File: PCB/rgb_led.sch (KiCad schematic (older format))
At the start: 4 parts

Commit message: PCB Edge.Cuts Defined
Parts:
- removed R? (x3): Resistor, symbol Resistor
- added C4: Capacitor, local:SMD-0805, symbol Capacitor
- D0: renamed from D?; footprint (none) -> local:T-1_5mm
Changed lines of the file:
@@
 EELAYER 26 0
 EELAYER END
-$Descr A4 11693 8268
+$Descr A 11000 8500
 encoding utf-8
-Sheet 5 5
-Title ""
-Date ""
-Rev ""
-Comp ""
+Sheet 12 20
+Title "Christmas Tree Disco"
+Date "2017-08-01"
+Rev "01"
+Comp "www.GitHub.com/Cryochasm"
 Comment1 ""
 Comment2 ""
@@
 $EndDescr
 $Comp
-L Resistor R?
-U 1 1 5980A851
-P 5200 3600
-F 0 "R?" H 5200 3450 50  0000 L CNN
-F 1 "Resistor" H 5050 3525 50  0000 L CNN
-F 2 "" H 5200 3600 60  0001 C CNN
-F 3 "" H 5200 3600 60  0001 C CNN
-F 4 "?" H 5200 3600 60  0001 C CNN "MPN"
-F 5 "?" H 5200 3600 60  0001 C CNN "Description"
-F 6 "Yes" H 5200 3600 60  0001 C CNN "Included in BOM"
-	1    5200 3600
-	0    1    1    0
-$EndComp
-$Comp
-L Resistor R?
-U 1 1 5980B065
-P 5400 3600
-F 0 "R?" H 5400 3500 50  0000 L CNN
-F 1 "Resistor" H 5275 3525 50  0000 L CNN
-F 2 "" H 5400 3600 60  0001 C CNN
-F 3 "" H 5400 3600 60  0001 C CNN
-F 4 "?" H 5400 3600 60  0001 C CNN "MPN"
-F 5 "?" H 5400 3600 60  0001 C CNN "Description"
-F 6 "Yes" H 5400 3600 60  0001 C CNN "Included in BOM"
-	1    5400 3600
-	0    1    1    0
-$EndComp
-$Comp
-L Resistor R?
-U 1 1 5980B07B
-P 5600 3600
-F 0 "R?" H 5600 3500 50  0000 L CNN
-F 1 "Resistor" H 5475 3525 50  0000 L CNN
-F 2 "" H 5600 3600 60  0001 C CNN
-F 3 "" H 5600 3600 60  0001 C CNN
-F 4 "?" H 5600 3600 60  0001 C CNN "MPN"
-F 5 "?" H 5600 3600 60  0001 C CNN "Description"
-F 6 "Yes" H 5600 3600 60  0001 C CNN "Included in BOM"
-	1    5600 3600
-	0    1    1    0
-$EndComp
-$Comp
-L LED_RGB_Common_Anode D?
+L LED_RGB_Common_Anode D0
 U 1 1 5980D97F
 P 5400 3300
-F 0 "D?" V 5354 3622 50  0000 L CNN
+AR Path="/59809489/5980966C/5980A64F/5980D97F" Ref="D0"  Part="1"
+AR Path="/59809489/5980966C/59813FE2/5980D97F" Ref="D4"  Part="1"
+AR Path="/59809489/5980966C/59815F66/5980D97F" Ref="D5"  Part="1"
+AR Path="/59809489/5980966C/5981626D/5980D97F" Ref="D2"  Part="1"
+AR Path="/59809489/5980966C/59817074/5980D97F" Ref="D3"  Part="1"
+AR Path="/59809489/5980966C/59817078/5980D97F" Ref="D6"  Part="1"
+AR Path="/59809489/5980966C/5981707C/5980D97F" Ref="D7"  Part="1"
+AR Path="/59809489/5980966C/59817080/5980D97F" Ref="D8"  Part="1"
+AR Path="/59809489/5980966C/59825578/5980D97F" Ref="D1"  Part="1"
+AR Path="/59809489/5980966C/598152C6/5980D97F" Ref="D9"  Part="1"
+AR Path="/59809489/5980966C/598152CA/5980D97F" Ref="D13"  Part="1"
+AR Path="/59809489/5980966C/59815DA2/5980D97F" Ref="D14"  Part="1"
+AR Path="/59809489/5980966C/59815DA6/5980D97F" Ref="D10"  Part="1"
+AR Path="/59809489/5980966C/59815DAA/5980D97F" Ref="D15"  Part="1"
+AR Path="/59809489/5980966C/598171EF/5980D97F" Ref="D11"  Part="1"
+AR Path="/59809489/5980966C/59837C41/5980D97F" Ref="D12"  Part="1"
+F 0 "D11" V 5354 3622 50  0000 L CNN
 F 1 "RGB LED" V 5445 3622 50  0000 L CNN
-F 2 "" H 5450 3300 60  0001 C CNN
+F 2 "local:T-1_5mm" H 5450 3300 60  0001 C CNN
 F 3 "https://media.digikey.com/pdf/Data%20Sheets/Kingbright%20PDFs/WP154A4SEJ3VBDZGW-CA_Ver.1A_Jul-24-13.pdf" H 5450 3300 60  0001 C CNN
 F 4 " WP154A4SEJ3VBDZGW/CA" H 5400 3300 60  0001 C CNN "MPN"
@@
 $EndComp
 Wire Wire Line
-	5200 3400 5200 3500
-Wire Wire Line
-	5400 3400 5400 3500
-Wire Wire Line
-	5600 3400 5600 3500
-Wire Wire Line
-	5400 3200 5400 3100
-Wire Wire Line
-	5200 3700 5200 3800
-Wire Wire Line
-	5400 3700 5400 3800
-Wire Wire Line
-	5600 3700 5600 3800
+	5400 3000 5400 3200
 Text HLabel 1100 2900 0    50   Input ~ 0
 ~~RGB[0..2]
-Text HLabel 1100 2400 0    50   BiDi ~ 0
+Text HLabel 1100 2400 0    50   Input ~ 0
 ~~POWER[0..1]
 Wire Bus Line
 	1100 2400 1200 2400
 Wire Bus Line
-	1200 2400 1200 2500
-Wire Bus Line
-	1200 2500 1200 2600
+	1200 2400 1200 2600
 Wire Bus Line
 	1100 2900 1200 2900
 Wire Bus Line
-	1200 2900 1200 3000
-Wire Bus Line
-	1200 3000 1200 3100
-Wire Bus Line
-	1200 3100 1200 3200
+	1200 2900 1200 3200
 Entry Wire Line
 	1200 2500 1300 2600
@@
 Text Label 1300 3300 0    50   ~ 0
 ~~RGB2
+Text Label 1700 3200 0    50   ~ 0
+RED
+Text Label 1700 3300 0    50   ~ 0
+GREEN
 Text Label 1700 3100 0    50   ~ 0
+BLUE
+Text Label 5600 3500 3    50   ~ 0
 RED
-Text Label 1700 3200 0    50   ~ 0
+Text Label 5200 3500 3    50   ~ 0
 GREEN
-Text Label 1700 3300 0    50   ~ 0
+Text Label 5400 3500 3    50   ~ 0
 BLUE
-Text Label 5600 3800 3    50   ~ 0
-RED
-Text Label 5200 3800 3    50   ~ 0
-GREEN
-Text Label 5400 3800 3    50   ~ 0
-BLUE
-Text Label 5400 3100 1    50   ~ 0
+Text Label 5400 3000 1    50   ~ 0
 5V
+$Comp
+L Capacitor C4
+U 1 1 598428D6
+P 4600 3300
+AR Path="/59809489/5980966C/59813FE2/598428D6" Ref="C4"  Part="1"
+AR Path="/59809489/5980966C/5980A64F/598428D6" Ref="C0"  Part="1"
+AR Path="/59809489/5980966C/59815F66/598428D6" Ref="C5"  Part="1"
+AR Path="/59809489/5980966C/59825578/598428D6" Ref="C1"  Part="1"
+AR Path="/59809489/5980966C/5981626D/598428D6" Ref="C2"  Part="1"
+AR Path="/59809489/5980966C/59817078/598428D6" Ref="C6"  Part="1"
+AR Path="/59809489/5980966C/59817074/598428D6" Ref="C3"  Part="1"
+AR Path="/59809489/5980966C/5981707C/598428D6" Ref="C7"  Part="1"
+AR Path="/59809489/5980966C/598171EF/598428D6" Ref="C11"  Part="1"
+AR Path="/59809489/5980966C/59815DAA/598428D6" Ref="C15"  Part="1"
+AR Path="/59809489/5980966C/59815DA6/598428D6" Ref="C10"  Part="1"
+AR Path="/59809489/5980966C/59815DA2/598428D6" Ref="C14"  Part="1"
+AR Path="/59809489/5980966C/598152CA/598428D6" Ref="C13"  Part="1"
+AR Path="/59809489/5980966C/598152C6/598428D6" Ref="C9"  Part="1"
+AR Path="/59809489/5980966C/59837C41/598428D6" Ref="C12"  Part="1"
+AR Path="/59809489/5980966C/59817080/598428D6" Ref="C8"  Part="1"
+F 0 "C11" V 4554 3368 50  0000 L CNN
+F 1 "Capacitor" V 4645 3368 50  0000 L CNN
+F 2 "local:SMD-0805" H 4600 3300 60  0001 C CNN
+F 3 "" H 4600 3300 60  0001 C CNN
+F 4 "?" H 4600 3300 60  0001 C CNN "MPN"
+F 5 "?" H 4600 3300 60  0001 C CNN "Description"
+F 6 "Yes" H 4600 3300 60  0001 C CNN "Included in BOM"
+	1    4600 3300
+	0    1    1    0
+$EndComp
+Wire Wire Line
+	5200 3400 5200 3500
+Wire Wire Line
+	5400 3400 5400 3500
+Wire Wire Line
+	5600 3400 5600 3500
+Wire Wire Line
+	5400 3100 4600 3100
+Wire Wire Line
+	4600 3100 4600 3200
+Connection ~ 5400 3100
+Wire Wire Line
+	4600 3400 4600 3500
+Text Label 4600 3500 3    50   ~ 0
+GND
 $EndSCHEMATC

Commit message: Preliminary PCB layout
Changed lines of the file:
@@
 $Descr A 11000 8500
 encoding utf-8
-Sheet 12 20
+Sheet 19 20
 Title "Christmas Tree Disco"
 Date "2017-08-01"
@@
 AR Path="/59809489/5980966C/598171EF/5980D97F" Ref="D11"  Part="1"
 AR Path="/59809489/5980966C/59837C41/5980D97F" Ref="D12"  Part="1"
-F 0 "D11" V 5354 3622 50  0000 L CNN
+F 0 "D13" V 5354 3622 50  0000 L CNN
 F 1 "RGB LED" V 5445 3622 50  0000 L CNN
 F 2 "local:T-1_5mm" H 5450 3300 60  0001 C CNN
@@
 AR Path="/59809489/5980966C/59837C41/598428D6" Ref="C12"  Part="1"
 AR Path="/59809489/5980966C/59817080/598428D6" Ref="C8"  Part="1"
-F 0 "C11" V 4554 3368 50  0000 L CNN
+F 0 "C13" V 4554 3368 50  0000 L CNN
 F 1 "Capacitor" V 4645 3368 50  0000 L CNN
 F 2 "local:SMD-0805" H 4600 3300 60  0001 C CNN

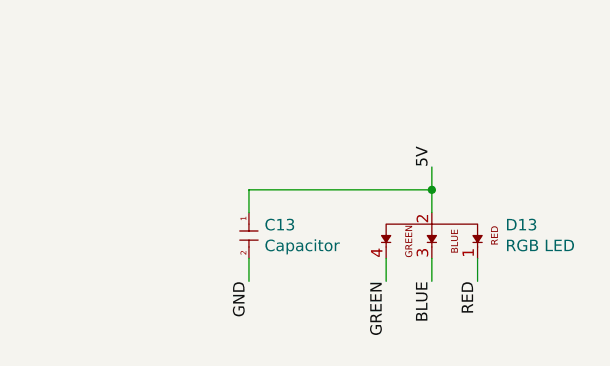
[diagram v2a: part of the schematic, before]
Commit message: PCB Layout
TODO: Change pinouts on dev kit to be compatable with Capacitive Touch
Audio booster pack.
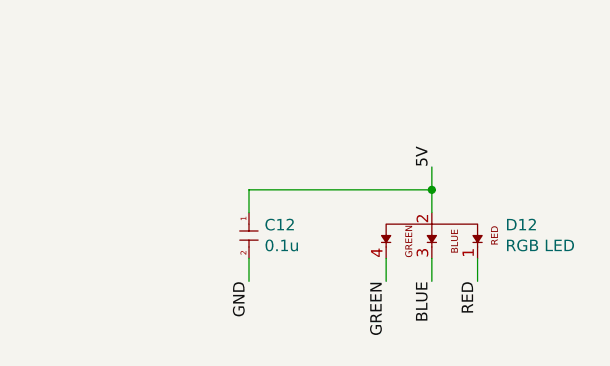
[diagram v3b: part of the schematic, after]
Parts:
- C4: value Capacitor -> 0.1u; Description ? -> 0.1µF ±10% 25V Ceramic Capacitor X7R 0805 (2012 Metric); MPN ? -> CL21B104KACWPNC
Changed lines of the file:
@@
 $Descr A 11000 8500
 encoding utf-8
-Sheet 19 20
+Sheet 13 20
 Title "Christmas Tree Disco"
 Date "2017-08-01"
@@
 AR Path="/59809489/5980966C/598171EF/5980D97F" Ref="D11"  Part="1"
 AR Path="/59809489/5980966C/59837C41/5980D97F" Ref="D12"  Part="1"
-F 0 "D13" V 5354 3622 50  0000 L CNN
+F 0 "D12" V 5354 3622 50  0000 L CNN
 F 1 "RGB LED" V 5445 3622 50  0000 L CNN
 F 2 "local:T-1_5mm" H 5450 3300 60  0001 C CNN
@@
 Text Label 5400 3000 1    50   ~ 0
 5V
-$Comp
-L Capacitor C4
-U 1 1 598428D6
-P 4600 3300
-AR Path="/59809489/5980966C/59813FE2/598428D6" Ref="C4"  Part="1"
-AR Path="/59809489/5980966C/5980A64F/598428D6" Ref="C0"  Part="1"
-AR Path="/59809489/5980966C/59815F66/598428D6" Ref="C5"  Part="1"
-AR Path="/59809489/5980966C/59825578/598428D6" Ref="C1"  Part="1"
-AR Path="/59809489/5980966C/5981626D/598428D6" Ref="C2"  Part="1"
-AR Path="/59809489/5980966C/59817078/598428D6" Ref="C6"  Part="1"
-AR Path="/59809489/5980966C/59817074/598428D6" Ref="C3"  Part="1"
-AR Path="/59809489/5980966C/5981707C/598428D6" Ref="C7"  Part="1"
-AR Path="/59809489/5980966C/598171EF/598428D6" Ref="C11"  Part="1"
-AR Path="/59809489/5980966C/59815DAA/598428D6" Ref="C15"  Part="1"
-AR Path="/59809489/5980966C/59815DA6/598428D6" Ref="C10"  Part="1"
-AR Path="/59809489/5980966C/59815DA2/598428D6" Ref="C14"  Part="1"
-AR Path="/59809489/5980966C/598152CA/598428D6" Ref="C13"  Part="1"
-AR Path="/59809489/5980966C/598152C6/598428D6" Ref="C9"  Part="1"
-AR Path="/59809489/5980966C/59837C41/598428D6" Ref="C12"  Part="1"
-AR Path="/59809489/5980966C/59817080/598428D6" Ref="C8"  Part="1"
-F 0 "C13" V 4554 3368 50  0000 L CNN
-F 1 "Capacitor" V 4645 3368 50  0000 L CNN
-F 2 "local:SMD-0805" H 4600 3300 60  0001 C CNN
-F 3 "" H 4600 3300 60  0001 C CNN
-F 4 "?" H 4600 3300 60  0001 C CNN "MPN"
-F 5 "?" H 4600 3300 60  0001 C CNN "Description"
-F 6 "Yes" H 4600 3300 60  0001 C CNN "Included in BOM"
-	1    4600 3300
-	0    1    1    0
-$EndComp
 Wire Wire Line
 	5200 3400 5200 3500
@@
 Text Label 4600 3500 3    50   ~ 0
 GND
+$Comp
+L Capacitor C4
+U 1 1 59893093
+P 4600 3300
+AR Path="/59809489/5980966C/59813FE2/59893093" Ref="C4"  Part="1"
+AR Path="/59809489/5980966C/5980A64F/59893093" Ref="C0"  Part="1"
+AR Path="/59809489/5980966C/59815F66/59893093" Ref="C5"  Part="1"
+AR Path="/59809489/5980966C/5981626D/59893093" Ref="C2"  Part="1"
+AR Path="/59809489/5980966C/59817074/59893093" Ref="C3"  Part="1"
+AR Path="/59809489/5980966C/59817078/59893093" Ref="C6"  Part="1"
+AR Path="/59809489/5980966C/5981707C/59893093" Ref="C7"  Part="1"
+AR Path="/59809489/5980966C/59825578/59893093" Ref="C1"  Part="1"
+AR Path="/59809489/5980966C/59837C41/59893093" Ref="C12"  Part="1"
+AR Path="/59809489/5980966C/598152C6/59893093" Ref="C9"  Part="1"
+AR Path="/59809489/5980966C/598152CA/59893093" Ref="C13"  Part="1"
+AR Path="/59809489/5980966C/59815DA2/59893093" Ref="C14"  Part="1"
+AR Path="/59809489/5980966C/59815DA6/59893093" Ref="C10"  Part="1"
+AR Path="/59809489/5980966C/59815DAA/59893093" Ref="C15"  Part="1"
+AR Path="/59809489/5980966C/598171EF/59893093" Ref="C11"  Part="1"
+F 0 "C12" V 4554 3368 50  0000 L CNN
+F 1 "0.1u" V 4645 3368 50  0000 L CNN
+F 2 "local:SMD-0805" H 4600 3300 60  0001 C CNN
+F 3 "http://www.samsungsem.com/kr/support/library/product-catalog/mlcc.jsp" H 4600 3300 60  0001 C CNN
+F 4 "CL21B104KACWPNC" H 4600 3300 60  0001 C CNN "MPN"
+F 5 "0.1µF ±10% 25V Ceramic Capacitor X7R 0805 (2012 Metric)" H 4600 3300 60  0001 C CNN "Description"
+F 6 "Yes" H 4600 3300 60  0001 C CNN "Included in BOM"
+	1    4600 3300
+	0    1    1    0
+$EndComp
 $EndSCHEMATC

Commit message: Gerber Updates
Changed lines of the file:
@@
 $Descr A 11000 8500
 encoding utf-8
-Sheet 13 20
+Sheet 19 20
 Title "Christmas Tree Disco"
 Date "2017-08-08"
-Rev "01"
+Rev "V1.0"
 Comp "www.GitHub.com/Cryochasm"
 Comment1 ""
@@
 AR Path="/59809489/5980966C/598171EF/5980D97F" Ref="D11"  Part="1"
 AR Path="/59809489/5980966C/59837C41/5980D97F" Ref="D12"  Part="1"
-F 0 "D12" V 5354 3622 50  0000 L CNN
+F 0 "D11" V 5354 3622 50  0000 L CNN
 F 1 "RGB LED" V 5445 3622 50  0000 L CNN
 F 2 "local:T-1_5mm" H 5450 3300 60  0001 C CNN
@@
 AR Path="/59809489/5980966C/59815DAA/59893093" Ref="C15"  Part="1"
 AR Path="/59809489/5980966C/598171EF/59893093" Ref="C11"  Part="1"
-F 0 "C12" V 4554 3368 50  0000 L CNN
+F 0 "C11" V 4554 3368 50  0000 L CNN
 F 1 "0.1u" V 4645 3368 50  0000 L CNN
 F 2 "local:SMD-0805" H 4600 3300 60  0001 C CNN

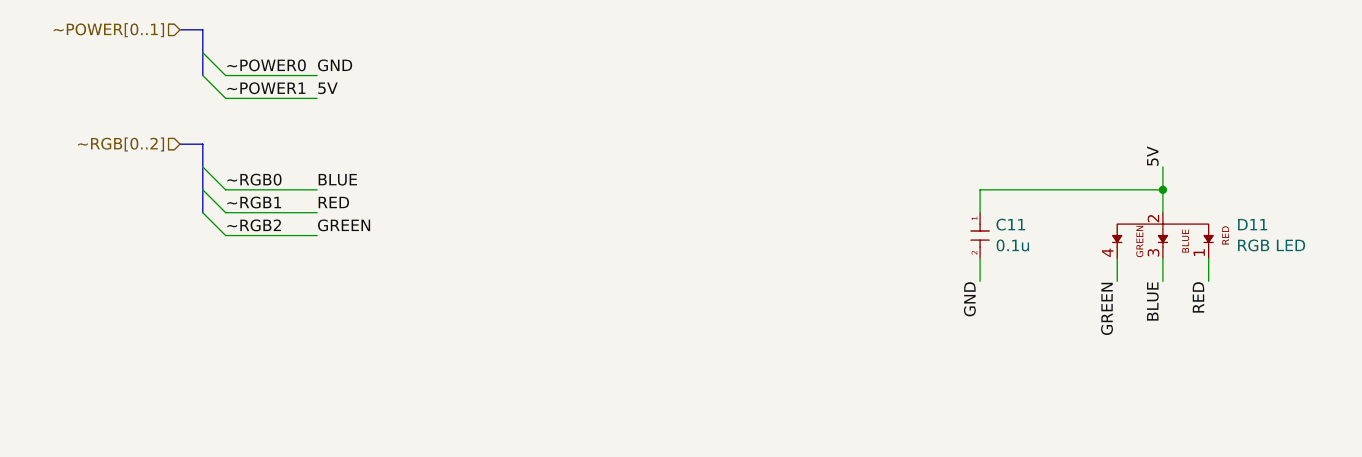
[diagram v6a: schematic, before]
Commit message: Removed Level Shifter, Cleaned up gerbers
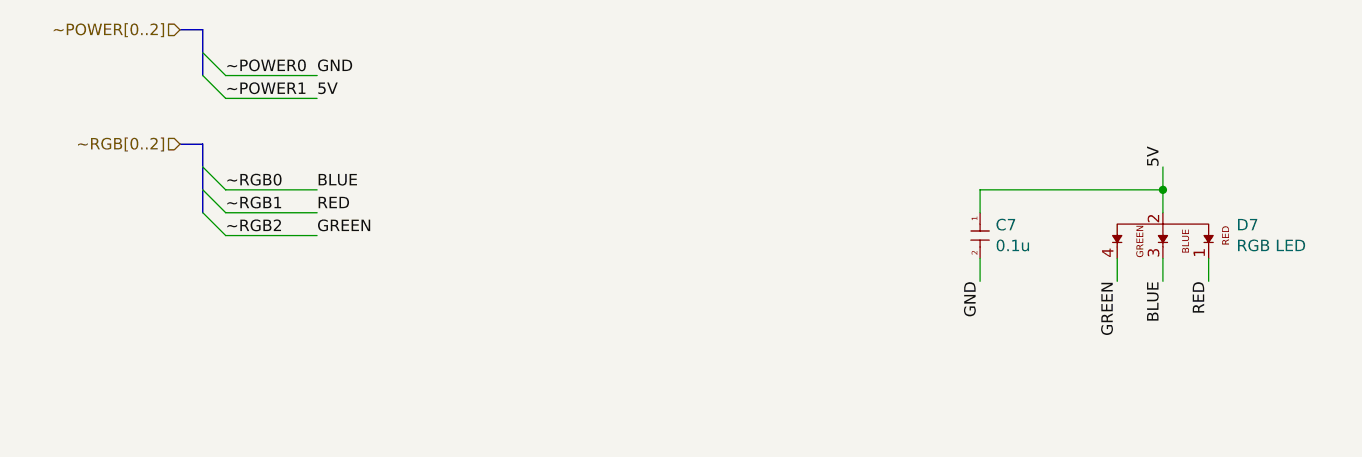
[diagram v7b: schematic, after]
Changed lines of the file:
@@
 $Descr A 11000 8500
 encoding utf-8
-Sheet 19 20
+Sheet 11 20
 Title "Christmas Tree Disco"
-Date "2017-08-15"
+Date "2017-08-23"
 Rev "V1.0"
 Comp "www.GitHub.com/Cryochasm"
@@
 AR Path="/59809489/5980966C/598171EF/5980D97F" Ref="D11"  Part="1"
 AR Path="/59809489/5980966C/59837C41/5980D97F" Ref="D12"  Part="1"
-F 0 "D11" V 5354 3622 50  0000 L CNN
+F 0 "D7" V 5354 3622 50  0000 L CNN
 F 1 "RGB LED" V 5445 3622 50  0000 L CNN
 F 2 "local:T-1_5mm" H 5450 3300 60  0001 C CNN
@@
 ~~RGB[0..2]
 Text HLabel 1100 2400 0    50   Input ~ 0
-~~POWER[0..1]
+~~POWER[0..2]
 Wire Bus Line
 	1100 2400 1200 2400
@@
 AR Path="/59809489/5980966C/59815DAA/59893093" Ref="C15"  Part="1"
 AR Path="/59809489/5980966C/598171EF/59893093" Ref="C11"  Part="1"
-F 0 "C11" V 4554 3368 50  0000 L CNN
+F 0 "C7" V 4554 3368 50  0000 L CNN
 F 1 "0.1u" V 4645 3368 50  0000 L CNN
 F 2 "local:SMD-0805" H 4600 3300 60  0001 C CNN
